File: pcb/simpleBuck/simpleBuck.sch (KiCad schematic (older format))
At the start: 21 parts, among them J2 Conn_01x06, J3 Conn_01x04, J4 Conn_01x02, J5 Conn_01x04, J6 Conn_01x02, U1 ANALOG_LTC1288CS8#PBF, U5 ANALOG_MAX539BCSA+, U6 ANALOG_MAX539BCSA+

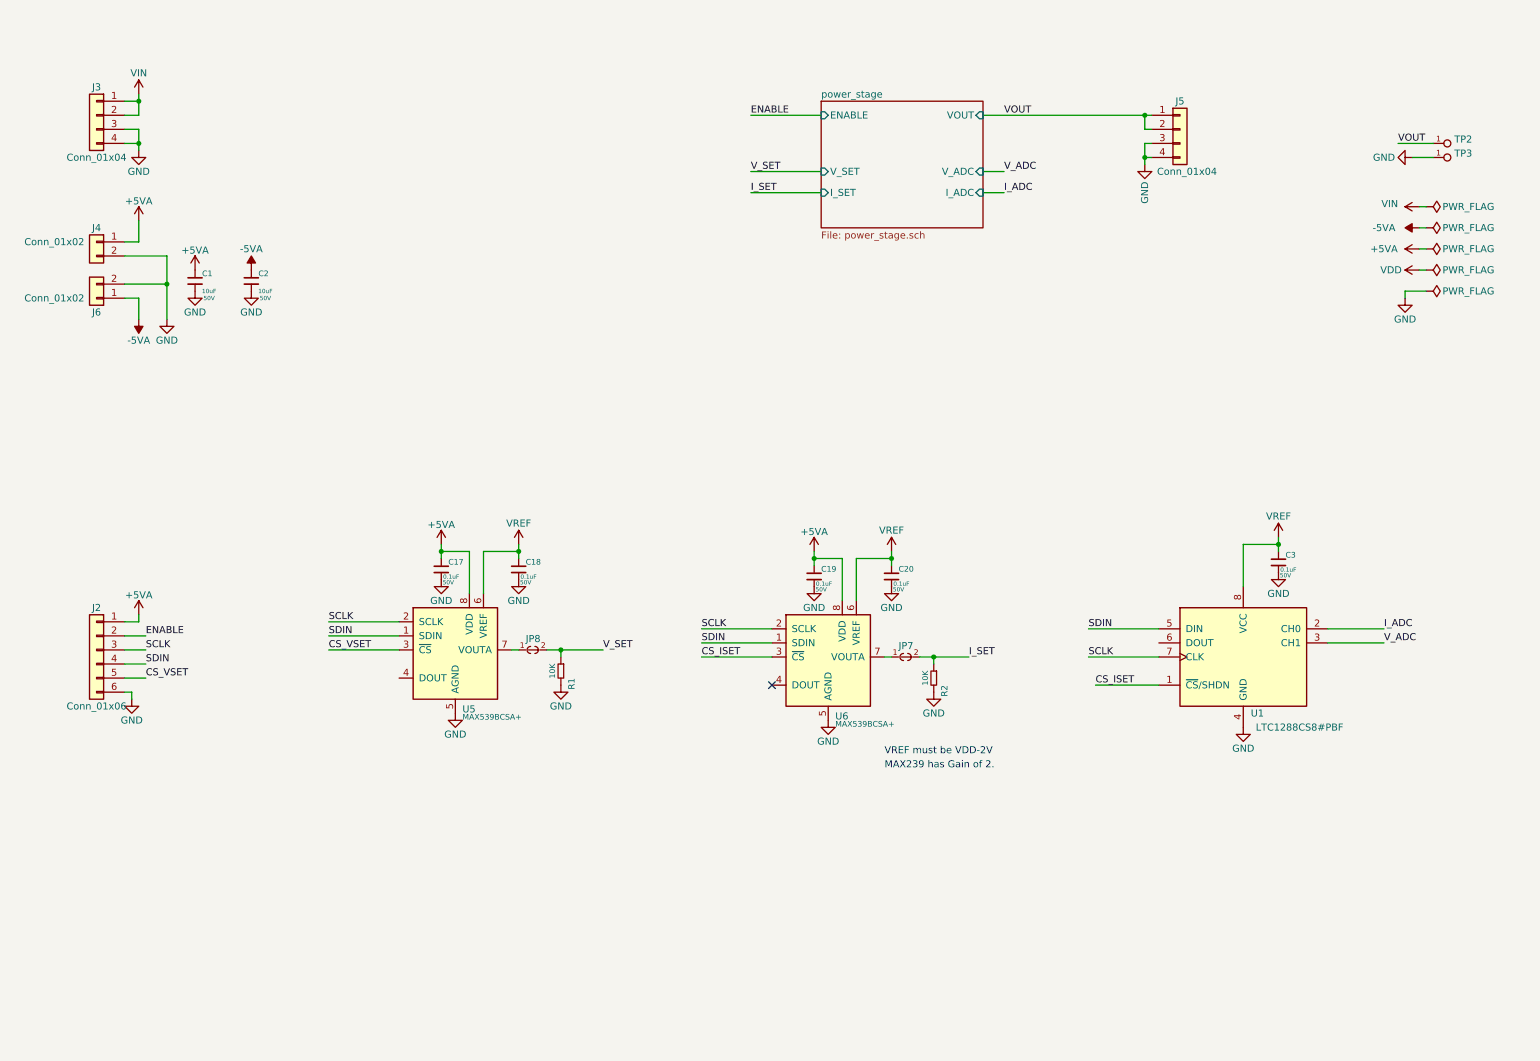
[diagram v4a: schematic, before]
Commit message: Added jumpers and finalized DAC/ADC selection.
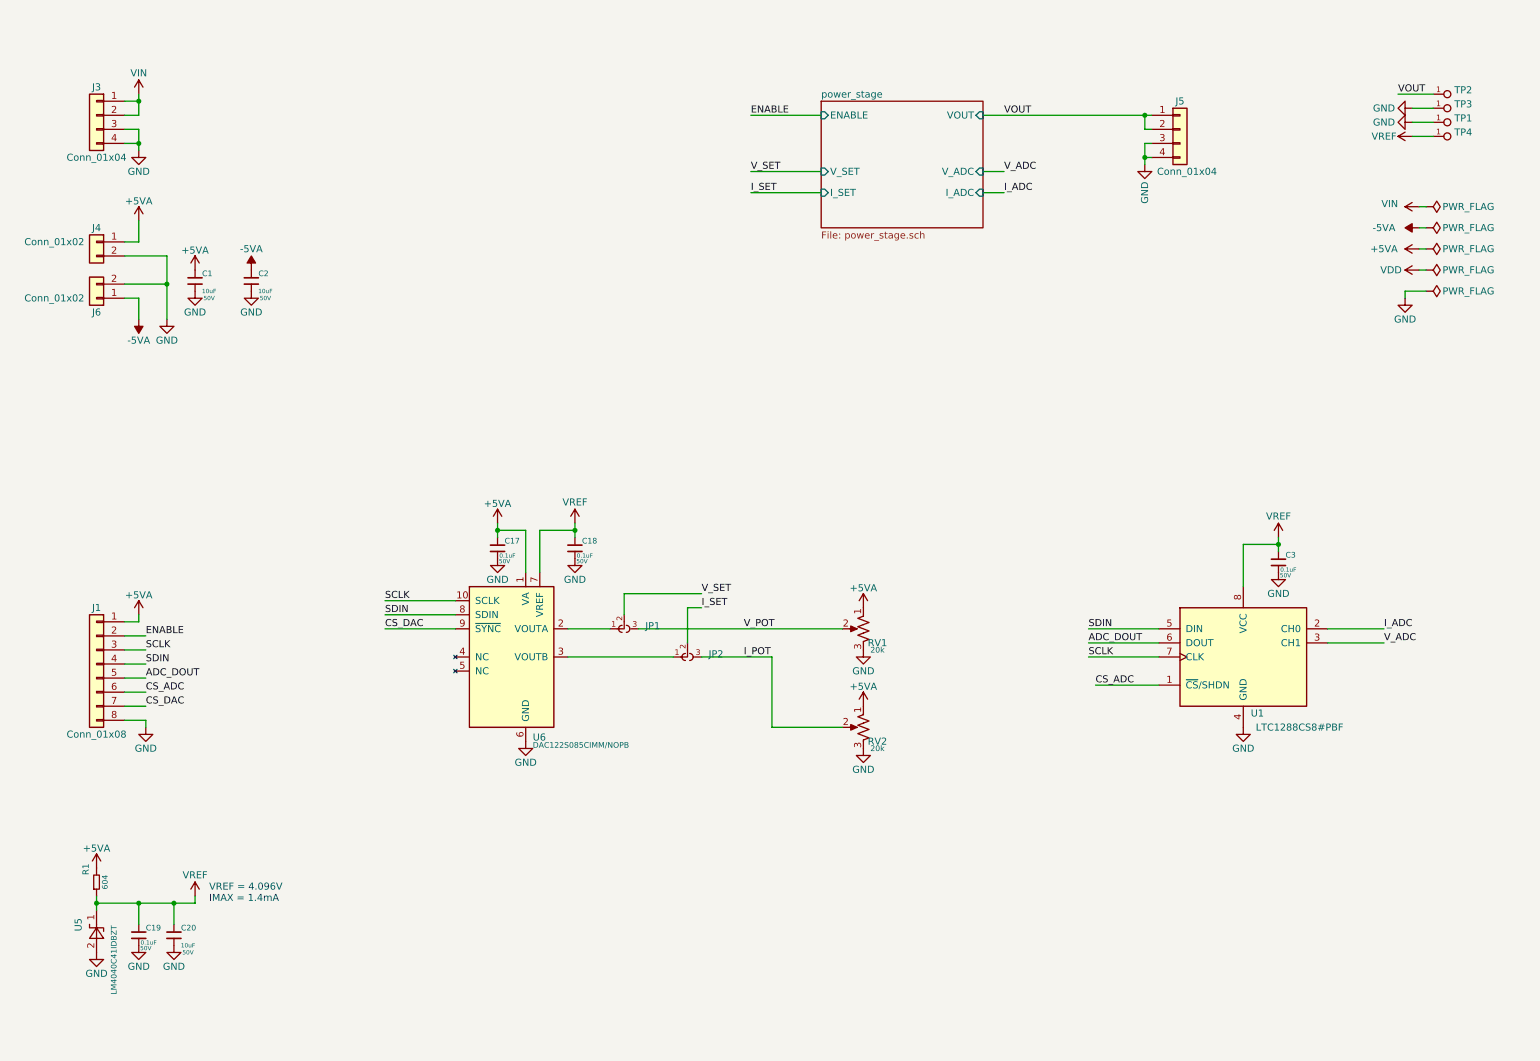
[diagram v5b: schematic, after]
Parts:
- removed C20: MURATA_GCJ188R91H104KA01D, Capacitors_SMD:C_0603, symbol DBLS_Capacitor:MURATA_GCJ188R91H104KA01D
- removed J2: Conn_01x06, Pin_Headers:Pin_Header_Straight_1x06_Pitch2.54mm, symbol Connector_Generic:Conn_01x06
- removed JP7, JP8: PAD_JUMPER_2PIN_0603, DBLS_Misc:PAD_JUMPER_2PIN_0603, symbol DBLS_Misc:PAD_JUMPER_2PIN_0603
- removed R1, R2: VISHAY_CRCW060310K0FKEBC, Resistors_SMD:R_0603, symbol DBLS_Resistor:VISHAY_CRCW060310K0FKEBC
- removed U5, U6: ANALOG_MAX539BCSA+, Housings_SOIC:SOIC-8_3.9x4.9mm_Pitch1.27mm, symbol DBLS_Data_Converters:ANALOG_MAX539BCSA+
- added C20: MURATA_GRT31CR61H106KE01L, Capacitors_SMD:C_1206, symbol DBLS_Capacitor:MURATA_GRT31CR61H106KE01L
- added J1: Conn_01x08, Pin_Headers:Pin_Header_Straight_1x08_Pitch2.54mm, symbol Connector_Generic:Conn_01x08
- added JP1, JP2: PAD_JUMPER_3PIN_12_NC_BY_TRACE, DBLS_Jumpers:PAD_JUMPER_3PIN_12_NC_BY_TRACE, symbol DBLS_Misc:PAD_JUMPER_3PIN_12_NC_BY_TRACE
- added R1: VISHAYDALE_CRCW0603604RFKEAHP, Resistors_SMD:R_0603, symbol DBLS_Resistor:VISHAYDALE_CRCW0603604RFKEAHP
- added RV1, RV2: BOURNS_PV37W203C01B00, Potentiometers:Potentiometer_Trimmer_Bourns_3299Y, symbol DBLS_Resistor:BOURNS_PV37W203C01B00
- added TP1, TP4: DBLS_TESTPOINT_NORMAL, DBLS_Misc:DBLS_Testpoint_Normal, symbol DBLS_Misc:DBLS_TESTPOINT_NORMAL
- added U5: TI_LM4040C41IDBZT, TO_SOT_Packages_SMD:SOT-23, symbol DBLS_Regulator:TI_LM4040C41IDBZT
- added U6: TI_DAC122S085CIMM_NOPB, Housings_SSOP:MSOP-10_3x3mm_Pitch0.5mm, symbol DBLS_Data_Converters:TI_DAC122S085CIMM_NOPB
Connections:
- net +5VA: now also J1.1 (Pin_1), R1.2, RV1.1, RV2.1, U6.1 (VA); no longer C19.1
- net ENABLE: now also J1.2 (Pin_2)
- net GND: now also C20.2, J1.8 (Pin_8), RV1.3, RV2.3, TP1.1, U5.2 (A), U6.6 (GND)
- net I_SET: now also JP2.2
- net SCLK: now also J1.3 (Pin_3), U6.10 (SCLK)
- net SDIN: now also J1.4 (Pin_4), U6.8 (SDIN)
- net VREF: now also C19.1, C20.1, R1.1, TP4.1, U5.1 (K), U6.7 (VREF)
- net V_SET: now also JP1.2
- net ADC_DOUT: now reaches U1.6 (DOUT)
- net ADC_DOUT: now also J1.5 (Pin_5)
- net CS_ISET renamed CS_ADC
- net CS_ADC: now also J1.6 (Pin_6)
- new net: JP1.1, U6.2 (VOUTA)
- new net: JP2.1, U6.3 (VOUTB)
- new net CS_DAC: J1.7 (Pin_7), U6.9 (~SYNC)
- new net I_POT: JP2.3, RV2.2
- new net V_POT: JP1.3, RV1.2
- no-connect marks 1 -> 0
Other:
- note added: "VREF = 4.096V\nIMAX = 1.4mA"
- note removed: "MAX239 has Gain of 2."
- note removed: "VREF must be VDD-2V"
- moved on the sheet: C17, C18, TP2, TP3

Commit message: Prelim Layout before silkscreen tuning.
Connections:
- net ADC_DOUT: now also J1.4 (Pin_4); no longer J1.5 (Pin_5)
- net CS_ADC: now also J1.7 (Pin_7); no longer J1.6 (Pin_6)
- net CS_DAC: now also J1.6 (Pin_6); no longer J1.7 (Pin_7)
- net SCLK: now also J1.5 (Pin_5); no longer J1.3 (Pin_3)
- net SDIN: now also J1.3 (Pin_3); no longer J1.4 (Pin_4)
- net at U6.2 (VOUTA): now also JP2.1; no longer JP1.1
- net at U6.3 (VOUTB): now also JP1.1; no longer JP2.1
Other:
- moved on the sheet: JP1, JP2, RV1, RV2
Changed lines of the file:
@@
 Connection ~ 3900 4100
 Connection ~ 4450 4100
-Text Label 1400 5050 0    50   ~ 0
+Text Label 1400 4950 0    50   ~ 0
 SDIN
-Text Label 1400 4950 0    50   ~ 0
+Text Label 1400 5150 0    50   ~ 0
 SCLK
 Text Label 1400 4850 0    50   ~ 0
@@
 Wire Wire Line
 	1250 4850 1400 4850
-Text Label 5350 4550 0    50   ~ 0
-V_SET
 Wire Wire Line
 	1250 5050 1400 5050
@@
 $EndComp
 $Comp
-L DBLS_Resistor:BOURNS_PV37W203C01B00 RV1
-U 1 1 6260CC0E
+L power:GND #PWR036
+U 1 1 6260CC1A
+P 6500 5650
+AR Path="/6260CC1A" Ref="#PWR036"  Part="1"
+AR Path="/620BD2D9/6260CC1A" Ref="#PWR?"  Part="1"
+AR Path="/625BEFFF/6260CC1A" Ref="#PWR?"  Part="1"
+F 0 "#PWR036" H 6500 5400 50  0001 C CNN
+F 1 "GND" H 6500 5500 50  0000 C CNN
+F 2 "" H 6500 5650 50  0001 C CNN
+F 3 "" H 6500 5650 50  0001 C CNN
+	1    6500 5650
+	1    0    0    -1
+$EndComp
+$Comp
+L DBLS_Resistor:BOURNS_PV37W203C01B00 RV2
+U 1 1 62616BEB
 P 6500 4800
-AR Path="/6260CC0E" Ref="RV1"  Part="1"
-AR Path="/625BEFFF/6260CC0E" Ref="RV?"  Part="1"
-F 0 "RV1" H 6400 4700 50  0000 C CNN
+AR Path="/62616BEB" Ref="RV2"  Part="1"
+AR Path="/625BEFFF/62616BEB" Ref="RV?"  Part="1"
+F 0 "RV2" H 6400 4700 50  0000 C CNN
 F 1 "BOURNS_PV37W203C01B00" V 6400 4800 50  0001 C CNN
 F 2 "Potentiometers:Potentiometer_Trimmer_Bourns_3299Y" H 6500 4800 50  0001 C CNN
@@
 $Comp
 L power:+5VA #PWR?
-U 1 1 6260CC14
+U 1 1 62616BF1
 P 6500 4650
-AR Path="/620BD2D9/6260CC14" Ref="#PWR?"  Part="1"
-AR Path="/6260CC14" Ref="#PWR031"  Part="1"
-AR Path="/625BEFFF/6260CC14" Ref="#PWR?"  Part="1"
-F 0 "#PWR031" H 6500 4500 50  0001 C CNN
+AR Path="/620BD2D9/62616BF1" Ref="#PWR?"  Part="1"
+AR Path="/62616BF1" Ref="#PWR037"  Part="1"
+AR Path="/625BEFFF/62616BF1" Ref="#PWR?"  Part="1"
+F 0 "#PWR037" H 6500 4500 50  0001 C CNN
 F 1 "+5VA" H 6500 4790 50  0000 C CNN
 F 2 "" H 6500 4650 50  0001 C CNN
@@
 $EndComp
 $Comp
-L power:GND #PWR036
-U 1 1 6260CC1A
+L power:GND #PWR048
+U 1 1 62616BF7
 P 6500 4950
-AR Path="/6260CC1A" Ref="#PWR036"  Part="1"
-AR Path="/620BD2D9/6260CC1A" Ref="#PWR?"  Part="1"
-AR Path="/625BEFFF/6260CC1A" Ref="#PWR?"  Part="1"
-F 0 "#PWR036" H 6500 4700 50  0001 C CNN
+AR Path="/62616BF7" Ref="#PWR048"  Part="1"
+AR Path="/620BD2D9/62616BF7" Ref="#PWR?"  Part="1"
+AR Path="/625BEFFF/62616BF7" Ref="#PWR?"  Part="1"
+F 0 "#PWR048" H 6500 4700 50  0001 C CNN
 F 1 "GND" H 6500 4800 50  0000 C CNN
 F 2 "" H 6500 4950 50  0001 C CNN
@@
 	1    0    0    -1
 $EndComp
-$Comp
-L DBLS_Misc:PAD_JUMPER_3PIN_12_NC_BY_TRACE JP1
-U 1 1 6260EEAC
-P 4800 4800
-F 0 "JP1" H 4950 4750 50  0000 L BNN
-F 1 "PAD_JUMPER_3PIN_12_NC_BY_TRACE" H 4850 4500 50  0001 C CNN
-F 2 "DBLS_Jumpers:PAD_JUMPER_3PIN_12_NC_BY_TRACE" H 4800 5000 50  0001 C CNN
-F 3 "" H 4800 5000 50  0001 C CNN
-F 4 "DNI" H 5000 4550 25  0001 C CNN "place"
-	1    4800 4800
-	1    0    0    1
-$EndComp
-$Comp
-L DBLS_Resistor:BOURNS_PV37W203C01B00 RV2
-U 1 1 62616BEB
-P 6500 5500
-AR Path="/62616BEB" Ref="RV2"  Part="1"
-AR Path="/625BEFFF/62616BEB" Ref="RV?"  Part="1"
-F 0 "RV2" H 6400 5400 50  0000 C CNN
-F 1 "BOURNS_PV37W203C01B00" V 6400 5500 50  0001 C CNN
-F 2 "Potentiometers:Potentiometer_Trimmer_Bourns_3299Y" H 6500 5500 50  0001 C CNN
-F 3 "https://www.bourns.com/docs/Product-Datasheets/pv37.pdf" H 6500 5500 50  0001 C CNN
-F 4 "Bourns Inc" H 6500 5500 50  0001 C CNN "mfg"
-F 5 "PV37W203C01B00" H 6500 5500 50  0001 C CNN "mfg_pn"
-F 6 "digikey" H 6500 5500 50  0001 C CNN "vendor"
-F 7 "490-2976-ND" H 6500 5500 50  0001 C CNN "vendor_pn"
-F 8 "yes" H 6500 5500 50  0001 C CNN "place"
-F 9 "20k" H 6400 5350 40  0000 C CNN "resistance"
-F 10 "TRIMMER 20K OHM 0.25W PC PIN TOP" H 6500 5500 50  0001 C CNN "description"
-	1    6500 5500
-	-1   0    0    -1
-$EndComp
-$Comp
-L power:+5VA #PWR?
-U 1 1 62616BF1
-P 6500 5350
-AR Path="/620BD2D9/62616BF1" Ref="#PWR?"  Part="1"
-AR Path="/62616BF1" Ref="#PWR037"  Part="1"
-AR Path="/625BEFFF/62616BF1" Ref="#PWR?"  Part="1"
-F 0 "#PWR037" H 6500 5200 50  0001 C CNN
-F 1 "+5VA" H 6500 5490 50  0000 C CNN
-F 2 "" H 6500 5350 50  0001 C CNN
-F 3 "" H 6500 5350 50  0001 C CNN
-	1    6500 5350
-	1    0    0    -1
-$EndComp
-$Comp
-L power:GND #PWR048
-U 1 1 62616BF7
-P 6500 5650
-AR Path="/62616BF7" Ref="#PWR048"  Part="1"
-AR Path="/620BD2D9/62616BF7" Ref="#PWR?"  Part="1"
-AR Path="/625BEFFF/62616BF7" Ref="#PWR?"  Part="1"
-F 0 "#PWR048" H 6500 5400 50  0001 C CNN
-F 1 "GND" H 6500 5500 50  0000 C CNN
-F 2 "" H 6500 5650 50  0001 C CNN
-F 3 "" H 6500 5650 50  0001 C CNN
-	1    6500 5650
-	1    0    0    -1
-$EndComp
-$Comp
-L DBLS_Misc:PAD_JUMPER_3PIN_12_NC_BY_TRACE JP2
-U 1 1 62617E21
-P 5250 5000
-F 0 "JP2" H 5400 4950 50  0000 L BNN
-F 1 "PAD_JUMPER_3PIN_12_NC_BY_TRACE" H 5300 4700 50  0001 C CNN
-F 2 "DBLS_Jumpers:PAD_JUMPER_3PIN_12_NC_BY_TRACE" H 5250 5200 50  0001 C CNN
-F 3 "" H 5250 5200 50  0001 C CNN
-F 4 "DNI" H 5450 4750 25  0001 C CNN "place"
-	1    5250 5000
-	1    0    0    1
-$EndComp
-Wire Wire Line
-	4700 4800 4400 4800
 Wire Wire Line
 	4400 5000 5150 5000
@@
 Wire Wire Line
 	5850 5500 6350 5500
-Wire Wire Line
-	6350 4800 4900 4800
-Wire Wire Line
-	5250 4900 5250 4650
-Wire Wire Line
-	5250 4650 5350 4650
-Wire Wire Line
-	4800 4700 4800 4550
-Wire Wire Line
-	4800 4550 5350 4550
-Text Label 5350 4650 0    50   ~ 0
-I_SET
-Text Label 5650 4800 0    50   ~ 0
-V_POT
-Text Label 5650 5000 0    50   ~ 0
+Text Label 5950 4800 0    50   ~ 0
 I_POT
 $Comp
@@
 	-1   0    0    -1
 $EndComp
+Text Label 1400 5250 0    50   ~ 0
+CS_DAC
 Text Label 1400 5350 0    50   ~ 0
-CS_DAC
-Text Label 1400 5250 0    50   ~ 0
 CS_ADC
 Wire Wire Line
@@
 Text Label 8100 4900 0    50   ~ 0
 ADC_DOUT
-Text Label 1400 5150 0    50   ~ 0
+Text Label 1400 5050 0    50   ~ 0
 ADC_DOUT
 $Comp
@@
 Wire Wire Line
 	10400 1300 10550 1300
+$Comp
+L DBLS_Misc:PAD_JUMPER_3PIN_12_NC_BY_TRACE JP2
+U 1 1 62617E21
+P 4800 4800
+F 0 "JP2" H 4950 4750 50  0000 L BNN
+F 1 "PAD_JUMPER_3PIN_12_NC_BY_TRACE" H 4850 4500 50  0001 C CNN
+F 2 "DBLS_Jumpers:PAD_JUMPER_3PIN_12_NC_BY_TRACE" H 4800 5000 50  0001 C CNN
+F 3 "" H 4800 5000 50  0001 C CNN
+F 4 "DNI" H 5000 4550 25  0001 C CNN "place"
+	1    4800 4800
+	1    0    0    1
+$EndComp
+$Comp
+L DBLS_Misc:PAD_JUMPER_3PIN_12_NC_BY_TRACE JP1
+U 1 1 6260EEAC
+P 5250 5000
+F 0 "JP1" H 5400 4950 50  0000 L BNN
+F 1 "PAD_JUMPER_3PIN_12_NC_BY_TRACE" H 5300 4700 50  0001 C CNN
+F 2 "DBLS_Jumpers:PAD_JUMPER_3PIN_12_NC_BY_TRACE" H 5250 5200 50  0001 C CNN
+F 3 "" H 5250 5200 50  0001 C CNN
+F 4 "DNI" H 5450 4750 25  0001 C CNN "place"
+	1    5250 5000
+	1    0    0    1
+$EndComp
+Text Label 6000 5500 0    50   ~ 0
+V_POT
+Text Label 5350 4550 0    50   ~ 0
+I_SET
+Wire Wire Line
+	4800 4550 5350 4550
+Wire Wire Line
+	4800 4700 4800 4550
+Wire Wire Line
+	5250 4650 5350 4650
+Wire Wire Line
+	5250 4900 5250 4650
+Wire Wire Line
+	6350 4800 4900 4800
+Wire Wire Line
+	4700 4800 4400 4800
+$Comp
+L power:+5VA #PWR?
+U 1 1 6260CC14
+P 6500 5350
+AR Path="/620BD2D9/6260CC14" Ref="#PWR?"  Part="1"
+AR Path="/6260CC14" Ref="#PWR031"  Part="1"
+AR Path="/625BEFFF/6260CC14" Ref="#PWR?"  Part="1"
+F 0 "#PWR031" H 6500 5200 50  0001 C CNN
+F 1 "+5VA" H 6500 5490 50  0000 C CNN
+F 2 "" H 6500 5350 50  0001 C CNN
+F 3 "" H 6500 5350 50  0001 C CNN
+	1    6500 5350
+	1    0    0    -1
+$EndComp
+$Comp
+L DBLS_Resistor:BOURNS_PV37W203C01B00 RV1
+U 1 1 6260CC0E
+P 6500 5500
+AR Path="/6260CC0E" Ref="RV1"  Part="1"
+AR Path="/625BEFFF/6260CC0E" Ref="RV?"  Part="1"
+F 0 "RV1" H 6400 5400 50  0000 C CNN
+F 1 "BOURNS_PV37W203C01B00" V 6400 5500 50  0001 C CNN
+F 2 "Potentiometers:Potentiometer_Trimmer_Bourns_3299Y" H 6500 5500 50  0001 C CNN
+F 3 "https://www.bourns.com/docs/Product-Datasheets/pv37.pdf" H 6500 5500 50  0001 C CNN
+F 4 "Bourns Inc" H 6500 5500 50  0001 C CNN "mfg"
+F 5 "PV37W203C01B00" H 6500 5500 50  0001 C CNN "mfg_pn"
+F 6 "digikey" H 6500 5500 50  0001 C CNN "vendor"
+F 7 "490-2976-ND" H 6500 5500 50  0001 C CNN "vendor_pn"
+F 8 "yes" H 6500 5500 50  0001 C CNN "place"
+F 9 "20k" H 6400 5350 40  0000 C CNN "resistance"
+F 10 "TRIMMER 20K OHM 0.25W PC PIN TOP" H 6500 5500 50  0001 C CNN "description"
+	1    6500 5500
+	-1   0    0    -1
+$EndComp
+Text Label 5350 4650 0    50   ~ 0
+V_SET
 $EndSCHEMATC

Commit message: Finished layout. Heading to fab
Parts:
- added LOGO1: DBLS_Chicken_Small, DBLS_LOGO:Rooster_4mmx4mm, symbol DBLS_Logo:DBLS_Chicken_Small
- added LOGO2: DBLS_van_logo_small_v1, DBLS_LOGO:van_logo_small, symbol DBLS_Logo:DBLS_van_logo_small_v1
- added LOGO3: DBLS_van_logo_8mmX6mm, DBLS_LOGO:van_logo_8mmX6mm, symbol DBLS_Logo:DBLS_van_logo_8mmX6mm
- added LOGO4: DBLS_van_logo_8mmX6mm_mirror, DBLS_LOGO:van_logo_8mmX6mm_mirror, symbol DBLS_Logo:DBLS_van_logo_8mmX6mm_mirror
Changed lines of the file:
@@
 Text Label 5350 4650 0    50   ~ 0
 V_SET
+$Comp
+L DBLS_Logo:DBLS_van_logo_small_v1 LOGO2
+U 1 1 6287A205
+P 6000 7450
+F 0 "LOGO2" H 6000 7450 50  0001 C CNN
+F 1 "DBLS_van_logo_small_v1" H 6000 7450 50  0001 C CNN
+F 2 "DBLS_LOGO:van_logo_small" H 6030 7600 20  0001 C CNN
+F 3 "" H 6000 7450 50  0001 C CNN
+F 4 "DNI" H 6000 7450 50  0001 C CNN "place"
+	1    6000 7450
+	1    0    0    -1
+$EndComp
+$Comp
+L DBLS_Logo:DBLS_Chicken_Small LOGO1
+U 1 1 6287A7A1
+P 5400 7450
+F 0 "LOGO1" H 5400 7450 50  0001 C CNN
+F 1 "DBLS_Chicken_Small" H 5400 7450 50  0001 C CNN
+F 2 "DBLS_LOGO:Rooster_4mmx4mm" H 5430 7600 20  0001 C CNN
+F 3 "" H 5400 7450 50  0001 C CNN
+F 4 "DNI" H 5400 7450 50  0001 C CNN "place"
+	1    5400 7450
+	1    0    0    -1
+$EndComp
+$Comp
+L DBLS_Logo:DBLS_van_logo_8mmX6mm LOGO3
+U 1 1 62886DDE
+P 6600 7450
+F 0 "LOGO3" H 6600 7450 50  0001 C CNN
+F 1 "DBLS_van_logo_8mmX6mm" H 6600 7450 50  0001 C CNN
+F 2 "DBLS_LOGO:van_logo_8mmX6mm" H 6630 7600 20  0001 C CNN
+F 3 "" H 6600 7450 50  0001 C CNN
+F 4 "DNI" H 6600 7450 50  0001 C CNN "place"
+	1    6600 7450
+	1    0    0    -1
+$EndComp
+$Comp
+L DBLS_Logo:DBLS_van_logo_8mmX6mm_mirror LOGO4
+U 1 1 6289FCE0
+P 6600 6800
+F 0 "LOGO4" H 6600 6800 50  0001 C CNN
+F 1 "DBLS_van_logo_8mmX6mm_mirror" H 6600 6800 50  0001 C CNN
+F 2 "DBLS_LOGO:van_logo_8mmX6mm_mirror" H 6630 6950 20  0001 C CNN
+F 3 "" H 6600 6800 50  0001 C CNN
+F 4 "DNI" H 6600 6800 50  0001 C CNN "place"
+	1    6600 6800
+	1    0    0    -1
+$EndComp
 $EndSCHEMATC
